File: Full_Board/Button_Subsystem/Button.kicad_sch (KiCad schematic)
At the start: 6 parts

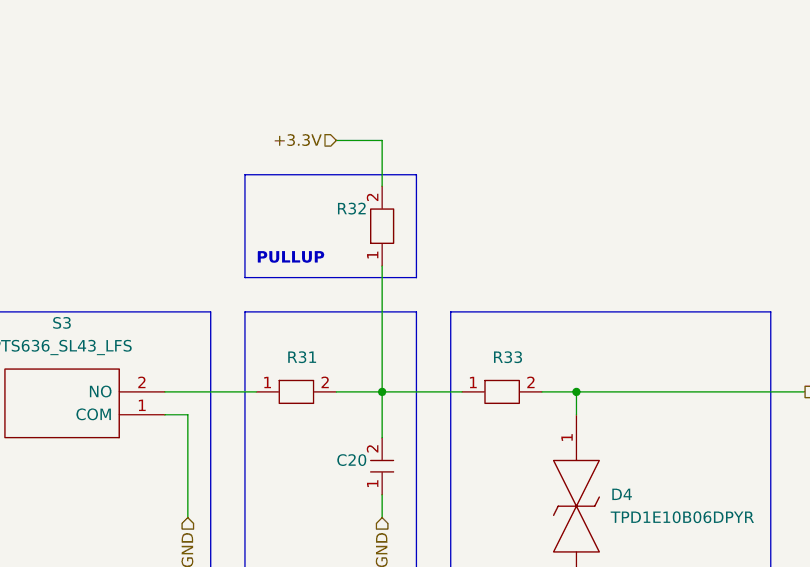
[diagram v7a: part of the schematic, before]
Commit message: Add footprints
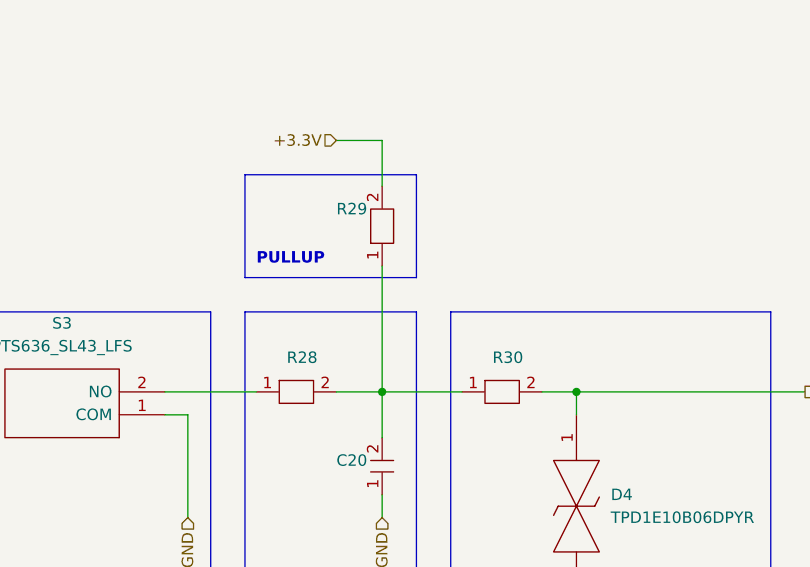
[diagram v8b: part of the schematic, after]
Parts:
- C20: footprint (none) -> C1210C822K2RACAUTO:CAPC3225X88N
- D4: footprint Diode_Protection_TPD1:TPD1E10B06DPYR -> TPD1E10B06DPYR:TPD1E10B06DPYR
- R28: renamed from R31; footprint Resistor_Chip_CR0402-FX-5620GLF:RESC1005X40N -> CR0402-FX-5620GLF:RESC1005X40N
- R29: renamed from R32; footprint Resistor_SMD:R_0201_0603Metric -> CRMA1210AF10K0DKEF:RESC3225X74N
- R30: renamed from R33; footprint (none) -> RCV2512100KFKEGAT:RESC6332X70N
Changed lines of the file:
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@@
     (effects (font (size 1.27 1.27)) (justify right))
   )
-  (symbol (lib_id "PTS636_SL43_LFS:PTS636_SL43_LFS") (at 129.54 97.79 180)
+  (symbol (lib_id "PTS636_SL43_LFS:PTS636_SL43_LFS") (at 129.54 97.79 180) (unit 1)
     (in_bom yes) (on_board yes) (fields_autoplaced)
     (property "Reference" "S3" (id 0) (at 118.11 87.63 0))
@@
     (pin "2")
   )
-  (symbol (lib_id "TPD1E10B06DPYR:TPD1E10B06DPYR") (at 175.26 97.79 270)
+  (symbol (lib_id "TPD1E10B06DPYR:TPD1E10B06DPYR") (at 175.26 97.79 270) (unit 1)
     (in_bom yes) (on_board yes)
     (property "Reference" "D4" (id 0) (at 179.07 106.68 90)
@@
       (effects (font (size 1.27 1.27)) (justify left))
     )
-    (property "Footprint" "Diode_Protection_TPD1:TPD1E10B06DPYR" (id 2) (at 179.07 110.49 0)
+    (property "Footprint" "TPD1E10B06DPYR:TPD1E10B06DPYR" (id 2) (at 179.07 110.49 0)
       (effects (font (size 1.27 1.27)) (justify left bottom) hide)
     )
@@
     (pin "2")
   )
-  (symbol (lib_id "C1210C822K2RACAUTO:C1210C822K2RACAUTO") (at 153.67 106.68 90)
+  (symbol (lib_id "C1210C822K2RACAUTO:C1210C822K2RACAUTO") (at 153.67 106.68 90) (unit 1)
     (in_bom yes) (on_board yes)
     (property "Reference" "C20" (id 0) (at 148.59 102.87 90)
@@
       (effects (font (size 1.27 1.27)) (justify right) hide)
     )
-    (property "Footprint" "" (id 2) (at 152.4 97.79 0)
+    (property "Footprint" "C1210C822K2RACAUTO:CAPC3225X88N" (id 2) (at 152.4 97.79 0)
       (effects (font (size 1.27 1.27)) (justify left) hide)
     )
@@
     (pin "2")
   )
-  (symbol (lib_id "CRMA1210AF10K0DKEF:CRMA1210AF10K0DKEF") (at 153.67 81.28 90)
+  (symbol (lib_id "CRMA1210AF10K0DKEF:CRMA1210AF10K0DKEF") (at 153.67 81.28 90) (unit 1)
     (in_bom yes) (on_board yes)
-    (property "Reference" "R32" (id 0) (at 148.59 74.93 90)
+    (property "Reference" "R29" (id 0) (at 148.59 74.93 90)
       (effects (font (size 1.27 1.27)) (justify right))
     )
@@
       (effects (font (size 1.27 1.27)) (justify right) hide)
     )
-    (property "Footprint" "Resistor_SMD:R_0201_0603Metric" (id 2) (at 152.4 67.31 0)
+    (property "Footprint" "CRMA1210AF10K0DKEF:RESC3225X74N" (id 2) (at 152.4 67.31 0)
       (effects (font (size 1.27 1.27)) (justify left) hide)
     )
@@
     (pin "2")
   )
-  (symbol (lib_id "RCV2512100KFKEGAT:RCV2512100KFKEGAT") (at 162.56 95.25 0)
+  (symbol (lib_id "RCV2512100KFKEGAT:RCV2512100KFKEGAT") (at 162.56 95.25 0) (unit 1)
     (in_bom yes) (on_board yes)
-    (property "Reference" "R33" (id 0) (at 167.64 91.44 0))
+    (property "Reference" "R30" (id 0) (at 167.64 91.44 0))
     (property "Value" "RCV2512100KFKEGAT" (id 1) (at 167.005 91.44 0)
       (effects (font (size 1.27 1.27)) hide)
     )
-    (property "Footprint" "" (id 2) (at 176.53 93.98 0)
+    (property "Footprint" "RCV2512100KFKEGAT:RESC6332X70N" (id 2) (at 176.53 93.98 0)
       (effects (font (size 1.27 1.27)) (justify left) hide)
     )
@@
     (pin "2")
   )
-  (symbol (lib_id "CR0402-FX-5620GLF:CR0402-FX-5620GLF") (at 139.7 95.25 0)
+  (symbol (lib_id "CR0402-FX-5620GLF:CR0402-FX-5620GLF") (at 139.7 95.25 0) (unit 1)
     (in_bom yes) (on_board yes)
-    (property "Reference" "R31" (id 0) (at 144.78 91.44 0))
+    (property "Reference" "R28" (id 0) (at 144.78 91.44 0))
     (property "Value" "CR0402-FX-5620GLF" (id 1) (at 144.145 91.44 0)
       (effects (font (size 1.27 1.27)) hide)
     )
-    (property "Footprint" "Resistor_Chip_CR0402-FX-5620GLF:RESC1005X40N" (id 2) (at 153.67 93.98 0)
+    (property "Footprint" "CR0402-FX-5620GLF:RESC1005X40N" (id 2) (at 153.67 93.98 0)
       (effects (font (size 1.27 1.27)) (justify left) hide)
     )
